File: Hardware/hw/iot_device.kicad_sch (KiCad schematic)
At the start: 19 parts, among them J4 Screw_Terminal_01x02, J6 Screw_Terminal_01x02, U1 ESP32-C6-WROOM-1, U2 RV-3028-C7, U5 TPS63001

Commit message: IoT update
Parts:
- removed J4, J6: Screw_Terminal_01x02, TerminalBlock_Phoenix:TerminalBlock_Phoenix_MPT-0,5-2-2.54_1x02_P2.54mm_Horizontal, symbol Connector:Screw_Terminal_01x02
- added R17, R18: 100R, Resistor_SMD:R_0805_2012Metric, symbol Device:R
- added U6: INA219, INA219_Module:MODULE_INA219, symbol INA219:INA219
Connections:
- net 3v3: now also C8.1, R17.1, R18.1, U6.1 (VCC); no longer C8.2
- net GND: now also C8.2, U6.2 (GND); no longer C8.1
- net I2C_SCL: now also R18.2, U6.3 (SCL)
- net I2C_SDA: now also R17.2, U6.4 (SDA)
- net GPIO21: now reaches U1.19 (GPIO21)
- net CHG: now reaches U1.20 (GPIO22)
- net FAULT: now reaches U1.21 (GPIO23)
- net LiPo renamed Vin-
- net Vin-: now also U6.5 (VIN-)
- new net Load: U6.6 (VIN+)
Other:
- moved on the sheet: C10, C2, C3, C4, C5, C8, C9, L2, R11, R12, R13, R14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

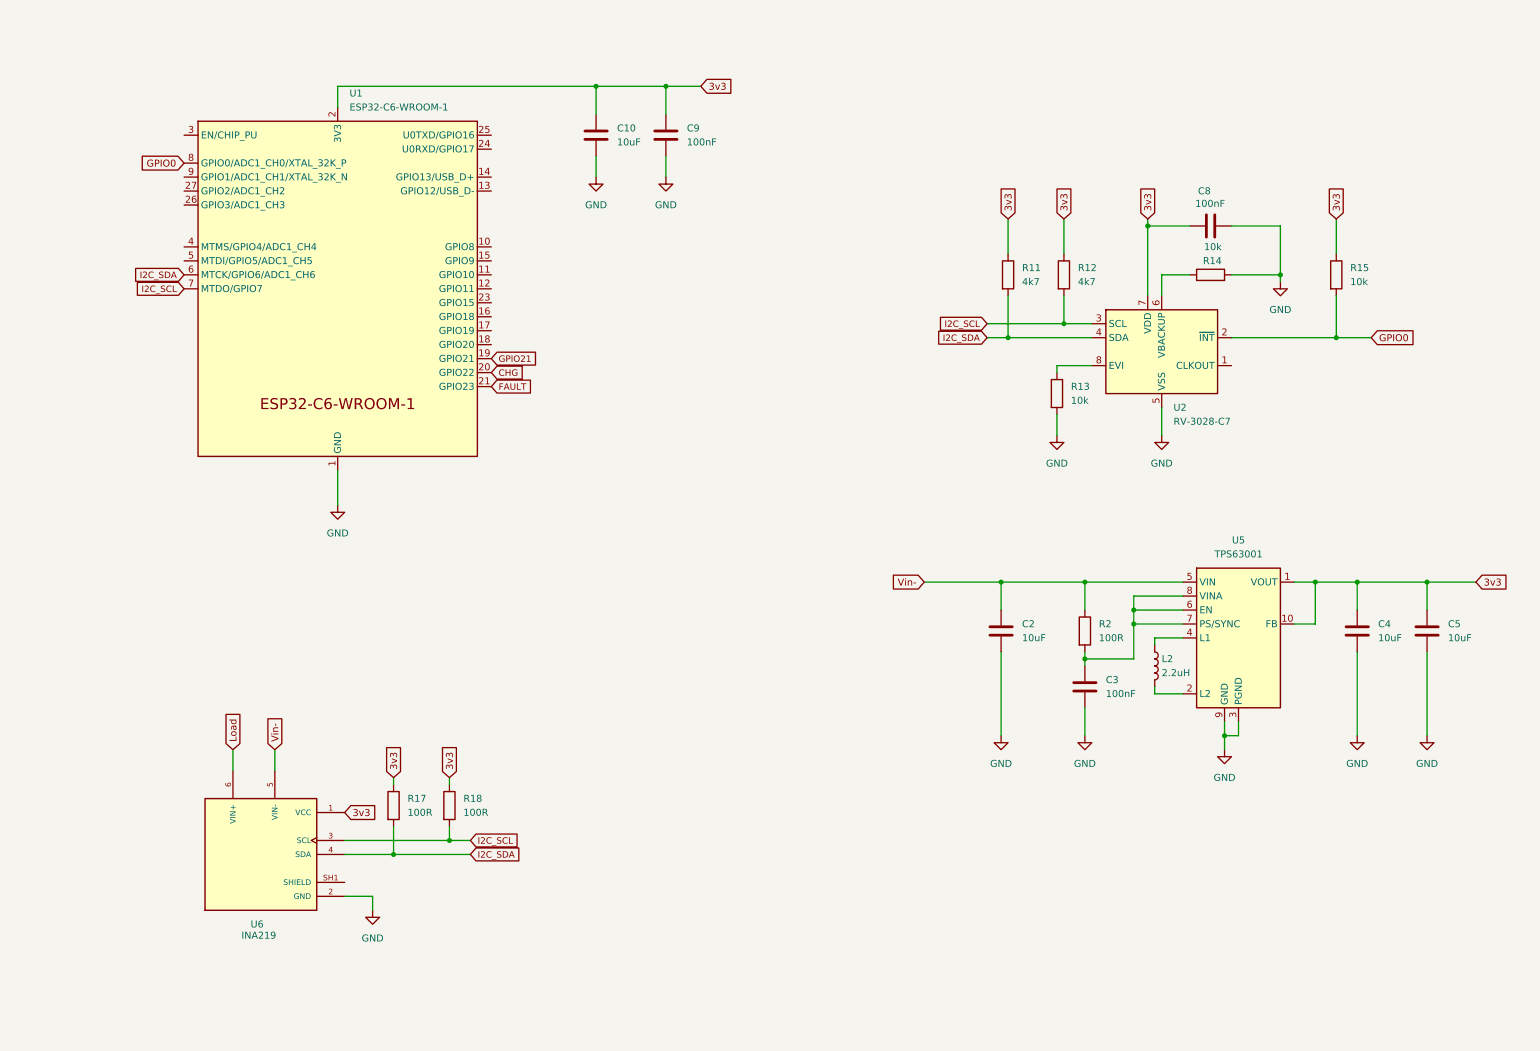
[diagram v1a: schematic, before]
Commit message: USB and UART update
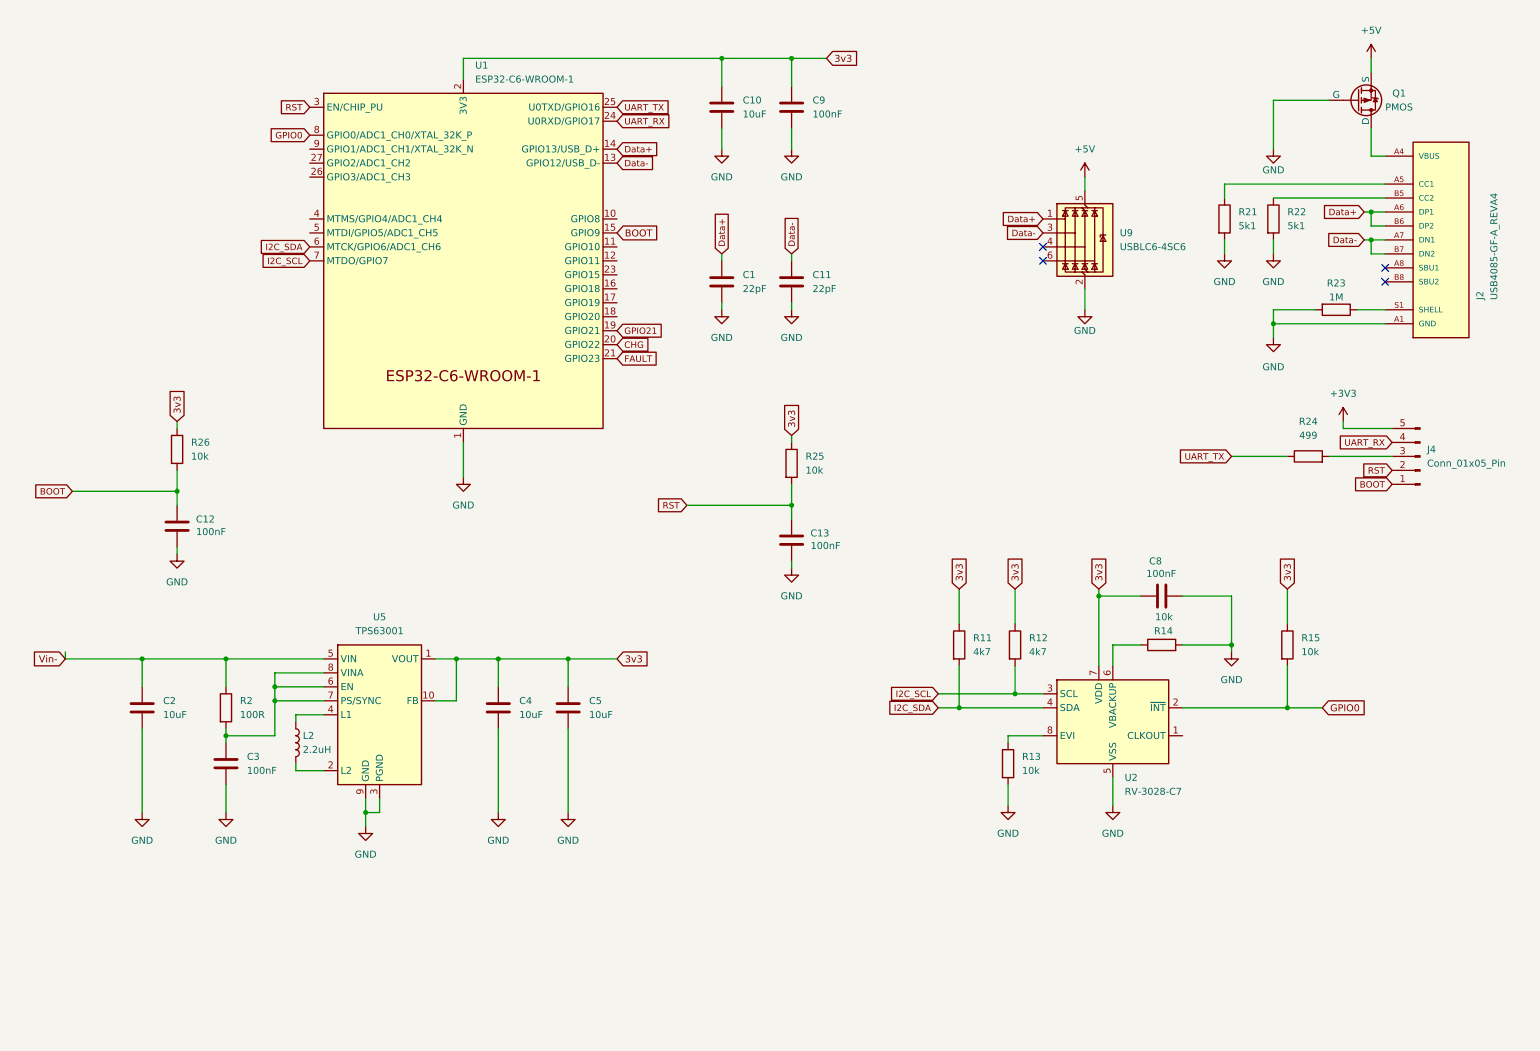
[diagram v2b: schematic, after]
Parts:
- removed R17, R18: 100R, Resistor_SMD:R_0805_2012Metric, symbol Device:R
- removed U6: INA219, INA219_Module:MODULE_INA219, symbol INA219:INA219
- added C1, C11: 22pF, Capacitor_SMD:C_0805_2012Metric, symbol Device:C
- added C12, C13: 100nF, Capacitor_SMD:C_0805_2012Metric, symbol Device:C
- added J2: USB4085-GF-A_REVA4, USB4085-GF-A_REVA4:GCT_USB4085-GF-A_REVA4, symbol USB4085-GF-A_REVA4:USB4085-GF-A_REVA4
- added J4: Conn_01x05_Pin, Connector_PinHeader_2.54mm:PinHeader_1x05_P2.54mm_Vertical, symbol Connector:Conn_01x05_Pin
- added Q1: PMOS, PMOS-SOT23:PMOS-SOT23, symbol Simulation_SPICE:PMOS
- added R21, R22: 5k1, Resistor_SMD:R_0805_2012Metric, symbol Device:R
- added R23: 1M, Resistor_SMD:R_0805_2012Metric, symbol Device:R
- added R24: 499, Resistor_SMD:R_0805_2012Metric, symbol Device:R
- added R25, R26: 10k, Resistor_SMD:R_0805_2012Metric, symbol Device:R
- added U9: USBLC6-4SC6, Package_TO_SOT_SMD:SOT-23-6, symbol Power_Protection:USBLC6-4SC6
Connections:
- net 3v3: now also R25.1, R26.1
- net GND: now also C1.2, C11.2, C12.2, C13.2, J2.A1 (GND), J2.A12 (GND), J2.B1 (GND), J2.B12 (GND), Q1.2 (G), R21.2, R22.2, R23.2, U9.2 (GND)
- net Data-: now reaches U1.13 (GPIO12/USB_D-)
- net Data-: now also C11.1, J2.A7 (DN1), J2.B7 (DN2), U9.3 (I/O2)
- net Data+: now reaches U1.14 (GPIO13/USB_D+)
- net Data+: now also C1.1, J2.A6 (DP1), J2.B6 (DP2), U9.1 (I/O1)
- net BOOT: now reaches U1.15 (GPIO9)
- net BOOT: now also C12.1, J4.1 (Pin_1), R26.2
- net UART_RX: now reaches U1.24 (U0RXD/GPIO17)
- net UART_RX: now also J4.4 (Pin_4)
- net UART_TX: now reaches U1.25 (U0TXD/GPIO16)
- net UART_TX: now also R24.1
- net RST: now reaches U1.3 (EN/CHIP_PU)
- net RST: now also C13.1, J4.2 (Pin_2), R25.2
- new net: J4.3 (Pin_3), R24.2
- new net: J2.S1 (SHELL), J2.S2 (SHELL), J2.S3 (SHELL), J2.S4 (SHELL), R23.1
- new net: J2.A5 (CC1), R21.1
- new net: J2.B5 (CC2), R22.1
- new net +3V3: J4.5 (Pin_5)
- new net +5V: Q1.3 (S), U9.5 (VBUS)
- new net VBUS: J2.A4 (VBUS), J2.A9 (VBUS), J2.B4 (VBUS), J2.B9 (VBUS), Q1.1 (D)
- no-connect marks 0 -> 4
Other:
- moved on the sheet: C10, C2, C3, C4, C5, C8, C9, L2, R11, R12, R13, R14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

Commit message: Big update
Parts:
- removed C13: 100nF, Capacitor_SMD:C_0805_2012Metric, symbol Device:C
- removed J4: Conn_01x05_Pin, Connector_PinHeader_2.54mm:PinHeader_1x05_P2.54mm_Vertical, symbol Connector:Conn_01x05_Pin
- added C14: 100nF, Capacitor_SMD:C_0805_2012Metric, symbol Device:C
- added J4: Conn_01x04_Pin, Connector_PinHeader_2.54mm:PinHeader_1x04_P2.54mm_Vertical, symbol Connector:Conn_01x04_Pin
- added Q7: PMOS, PMOS-SOT23:PMOS-SOT23, symbol Simulation_SPICE:PMOS
- added R27: 100k, Resistor_SMD:R_0805_2012Metric, symbol Device:R
- added R28: 10k, Resistor_SMD:R_0805_2012Metric, symbol Device:R
- added R29: 220, Resistor_SMD:R_0805_2012Metric, symbol Device:R
- added SW1, SW2: SW_Push, symbol Switch:SW_Push
- R25: value 10k -> 220
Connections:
- net Vin- is gone; now on net +5V: C2.1, R2.1, U5.5 (VIN)
- net +3V3: now also C10.1, C4.1, C5.1, C8.1, C9.1, R11.1, R12.1, R15.1, R26.1, U1.2 (3V3), U2.7 (VDD), U5.1 (VOUT), U5.10 (FB), R27.1, R28.1
- net +5V: now also Q7.3 (S)
- net BOOT: now also R28.2, R29.1; no longer R26.2
- net GND: now also C14.2, J4.1 (Pin_1), Q7.2 (G), SW1.2, SW2.2
- net RST: now also R25.1, R26.2, C14.1; no longer R25.2
- net UART_RX: now also U9.4 (I/O3), J4.3 (Pin_3)
- net UART_TX: now also U9.6 (I/O4)
- net at R24.2: now also J4.2 (Pin_2)
- net GPIO8: now reaches U1.10 (GPIO8)
- net GPIO8: now also R27.2
- net GPIO10: now reaches U1.11 (GPIO10)
- removed net 3v3: C10.1, C4.1, C5.1, C8.1, C9.1, R11.1, R12.1, R15.1, R25.1, R26.1, U1.2 (3V3), U2.7 (VDD), U5.1 (VOUT), U5.10 (FB)
- new net: R29.2, SW1.1
- new net: R25.2, SW2.1
- new net: J4.4 (Pin_4), Q7.1 (D)
- no-connect marks 4 -> 2
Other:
- moved on the sheet: C1, C11, C2, C3, C4, C5, C8, L2, R11, R12, R13, R14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

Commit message: little update
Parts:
- added J7: Conn_01x02_Pin, Connector_PinHeader_2.54mm:PinHeader_1x02_P2.54mm_Vertical, symbol Connector:Conn_01x02_Pin
- SW1, SW2: footprint (none) -> Button_Switch_THT:SW_PUSH_6mm
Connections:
- net GPIO8: now also J7.2 (Pin_2); no longer R27.2
- new net: J7.1 (Pin_1), R27.2
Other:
- moved on the sheet: C12, C14, R25, R26, R27, R28, R29, SW1, SW2

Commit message: Sensors update
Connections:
- net ADC3: now reaches U1.26 (GPIO3/ADC1_CH3)
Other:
- moved on the sheet: C1, C10, C11, C12, C14, C2, C3, C4, C5, C8, C9, J2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

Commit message: Hardware v1.0
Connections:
- net GPIO12: now reaches U1.12 (GPIO11)
- net GPIO18: now reaches U1.16 (GPIO18)
- net GPIO19: now reaches U1.17 (GPIO19)
- net GPIO20: now reaches U1.18 (GPIO20)
- net GPIO15: now reaches U1.23 (GPIO15)
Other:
- note added: "Buttons"
- note added: "CPU"
- note added: "DC-to-DC Converter"
- note added: "External RTC"
- note added: "USB-C and UART"
- company: (none) -> UNIZA Faculty of Management Science and Informatics Department of Technical Cybernetics
- title: (none) -> Solar Power Management and Monitoring Circuit
- moved on the sheet: C1, C11, C12, C14, C8, J2, J4, J7, Q1, Q7, R11, R12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

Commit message: External ADC update
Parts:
- removed J7: Conn_01x02_Pin, Connector_PinHeader_2.54mm:PinHeader_1x02_P2.54mm_Vertical, symbol Connector:Conn_01x02_Pin
- removed R11, R12: 4k7, Resistor_SMD:R_0805_2012Metric, symbol Device:R
- added JP1: Jumper_2_Open, TestPoint:TestPoint_2Pads_Pitch2.54mm_Drill0.8mm, symbol Jumper:Jumper_2_Open
- added R17, R18: 4k7, Resistor_SMD:R_0805_2012Metric, symbol Device:R
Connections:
- net +3V3: now also R17.1, R18.1
- net GPIO8: now also JP1.1 (A)
- net I2C_SCL: now also R18.2
- net I2C_SDA: now also R17.2
- net at R27.2: now also JP1.2 (B)
- net ADC3: no longer names the net of U1.26 (GPIO3/ADC1_CH3)
- no-connect marks 2 -> 8
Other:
- moved on the sheet: R27

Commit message: Tomáš update
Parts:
- removed C1: 22pF, Capacitor_SMD:C_0805_2012Metric, symbol Device:C
- removed JP1: Jumper_2_Open, TestPoint:TestPoint_2Pads_Pitch2.54mm_Drill0.8mm, symbol Jumper:Jumper_2_Open
- removed R13, R14: 10k, Resistor_SMD:R_0805_2012Metric, symbol Device:R
- added C15: 1nF, Capacitor_SMD:C_0805_2012Metric, symbol Device:C
- added R30: 100, Resistor_SMD:R_0805_2012Metric, symbol Device:R
- C11: value 22pF -> 1uF
- R24: value 499 -> 100
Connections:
- net +3V3: now also C11.1, U2.6 (VBACKUP)
- net Data-: no longer C11.1
- net GND: now also R23.1, C15.2; no longer R23.2
- net GPIO8: now also R27.2
- net UART_RX: now also R30.1; no longer J4.3 (Pin_3)
- net at J2.S1 (SHELL), J2.S2 (SHELL), J2.S3 (SHELL)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: now also R23.2, C15.1; no longer R23.1
- new net: J4.3 (Pin_3), R30.2
- no-connect marks 8 -> 9
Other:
- moved on the sheet: C10, C12, C14, C8, C9, R23, R24, R25, R26, R27, R28, R29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
